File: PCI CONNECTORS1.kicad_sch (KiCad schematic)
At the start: 13 parts, among them J36 PCI1, J37 PCI1

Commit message: page 18 ISA, small fixes
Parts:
- removed J36, J37: PCI1, P2-3_ERA:PCI_GENERIC, symbol P2-3_era:PCI_Generic_1
- added J36, J37: PCI_CONN, custom:PCI1, symbol P2-3_era:PCI_Slot
- C18, C19, C20, C21: value 0.1uf 16v -> 0.1uf
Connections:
- net AD29 is gone; now on net AD1: R68.2
- net AD31 is gone; now on net AD1: R71.2
- net AD0: now also J36.A20 (AD(30)), J36.A22 (AD(28)), J36.A23 (AD(26)), J36.A25 (AD(24)), J36.A28 (AD(22)), J36.A29 (AD(20)), J36.A31 (AD(18)), J36.A32 (AD(16)), J36.A44 (AD(15)), J36.A46 (AD(13)), J36.A47 (AD(11)), J36.A49 (AD(09)), J36.A54 (AD(06)), J36.A55 (AD(04)), J36.A57 (AD(02)), J36.A58 (AD(00)), J37.A20 (AD(30)), J37.A22 (AD(28)), J37.A23 (AD(26)), J37.A25 (AD(24)), J37.A28 (AD(22)), J37.A29 (AD(20)), J37.A31 (AD(18)), J37.A32 (AD(16)), J37.A44 (AD(15)), J37.A46 (AD(13)), J37.A47 (AD(11)), J37.A49 (AD(09)), J37.A54 (AD(06)), J37.A55 (AD(04)), J37.A57 (AD(02)), J37.A58 (AD(00))
- net AD1: now also J36.B20 (AD(31)), J36.B21 (AD(29)), J36.B23 (AD(27)), J36.B24 (AD(25)), J36.B27 (AD(23)), J36.B29 (AD(21)), J36.B30 (AD(19)), J36.B32 (AD(17)), J36.B45 (AD(14)), J36.B47 (AD(12)), J36.B48 (AD(10)), J36.B52 (AD(8)), J36.B53 (AD(7)), J36.B55 (AD(5)), J36.B56 (AD(3)), J36.B58 (AD(1)), J37.B20 (AD(31)), J37.B21 (AD(29)), J37.B23 (AD(27)), J37.B24 (AD(25)), J37.B27 (AD(23)), J37.B29 (AD(21)), J37.B30 (AD(19)), J37.B32 (AD(17)), J37.B45 (AD(14)), J37.B47 (AD(12)), J37.B48 (AD(10)), J37.B52 (AD(8)), J37.B53 (AD(7)), J37.B55 (AD(5)), J37.B56 (AD(3)), J37.B58 (AD(1))
- net C/BE#(0): now also J36.A52 (C/BE#(0)), J37.A52 (C/BE#(0))
- net C/BE#(1): now also J36.B26 (C/BE#(3)), J36.B33 (C/BE#(2)), J36.B44 (C/BE#(1)), J37.B26 (C/BE#(3)), J37.B33 (C/BE#(2)), J37.B44 (C/BE#(1))
- net DEVSEL#: now also J36.B37 (DEVSEL#), J37.B37 (DEVSEL#)
- net FRAME#: now also J36.A34 (FRAME#), J37.A34 (FRAME#)
- net IRDY#: now also J36.B35 (IRDY#), J37.B35 (IRDY#)
- net PAR: now also J36.A43 (PAR), J37.A43 (PAR)
- net PCIRST#: now also J36.A15 (RESET#), J37.A15 (RESET#)
- net PCI_PME#: now also J36.A19 (PME#), J37.A19 (PME#)
- net PCLK3: now also J36.B16 (CLK)
- net PCLK4: now also J37.B16 (CLK)
- net PERR#: now also J36.B40 (PERR#), J37.B40 (PERR#)
- net PGNT#2: now also J36.A17 (GNT#)
- net PGNT#3: now also J37.A17 (GNT#)
- net PIRQ#A: now also J36.A7 (INTC#), J37.B7 (INTB#)
- net PIRQ#B: now also J36.B8 (INTD#), J37.A7 (INTC#)
- net PIRQ#C: now also J36.A6 (INTA#), J37.B8 (INTD#)
- net PIRQ#D: now also J36.B7 (INTB#), J37.A6 (INTA#)
- net PLOCK#: now also J36.B39 (LOCK#), J37.B39 (LOCK#)
- net PREQ#2: now also J36.B18 (REQ#)
- net PREQ#3: now also J37.B18 (REQ#)
- net PRSNT#31: now also J36.B9 (PRSNT1#)
- net PRSNT#32: now also J36.B11 (PRSNT2#)
- net PRSNT#41: now also J37.B9 (PRSNT1#)
- net PRSNT#42: now also J37.B11 (PRSNT2#)
- net PTCK: now also J36.B2 (TCK), J37.B2 (TCK)
- net PTDI: now also J36.A4 (TDI), J37.A4 (TDI)
- net PTMS: now also J36.A3 (TMS), J37.A3 (TMS)
- net PTRST#: now also J36.A1 (TRST#), J37.A1 (TRST#)
- net PU3_ACK64#: now also J36.A60 (REQ64#)
- net PU3_REQ64#: now also J36.B60 (ACK64#)
- net PU4_REQ64#: now also J37.B60 (ACK64#)
- net R_AD29: now also J36.A26 (IDSEL)
- net R_AD31: now also J37.A26 (IDSEL)
- net SBOP3: now also J36.A41 (SBO#)
- net SBOP4: now also J37.A41 (SBO#)
- net SDONEP3: now also J36.A40 (SDONE)
- net SDONEP4: now also J37.A40 (SDONE)
- net SERR#: now also J36.B42 (SERR#), J37.B42 (SERR#)
- net STOP#: now also J36.A38 (STOP#), J37.A38 (STOP#)
- net TRDY#: now also J36.A36 (TRDY#), J37.A36 (TRDY#)
- net Earth renamed GND
- net GND: now also J36.A12 (GND), J36.A13 (GND), J36.A18 (GND), J36.A24 (GND), J36.A30 (GND), J36.A35 (GND), J36.A37 (GND), J36.A42 (GND), J36.A48 (GND), J36.A56 (GND), J36.B12 (GND), J36.B13 (GND), J36.B15 (GND), J36.B17 (GND), J36.B22 (GND), J36.B28 (GND), J36.B3 (GND), J36.B34 (GND), J36.B38 (GND), J36.B46 (GND), J36.B49 (GND), J36.B57 (GND), J37.A12 (GND), J37.A13 (GND), J37.A18 (GND), J37.A24 (GND), J37.A30 (GND), J37.A35 (GND), J37.A37 (GND), J37.A42 (GND), J37.A48 (GND), J37.A56 (GND), J37.B12 (GND), J37.B13 (GND), J37.B15 (GND), J37.B17 (GND), J37.B22 (GND), J37.B28 (GND), J37.B3 (GND), J37.B34 (GND), J37.B38 (GND), J37.B46 (GND), J37.B49 (GND), J37.B57 (GND); no longer R70.2
- new net: J36.A10 (+5V), J36.A16 (+5V), J36.A5 (+5V), J36.A59 (+5V), J36.A61 (+5V), J36.A62 (+5V), J36.A8 (+5V)
- new net: J36.A21 (+3.3V), J36.A27 (+3.3V), J36.A33 (+3.3V), J36.A39 (+3.3V), J36.A45 (+3.3V), J36.A53 (+3.3V)
- new net: J36.B19 (+5V), J36.B5 (+5V), J36.B59 (+5V), J36.B6 (+5V), J36.B61 (+5V), J36.B62 (+5V)
- new net: J36.B25 (+3.3V), J36.B31 (+3.3V), J36.B36 (+3.3V), J36.B41 (+3.3V), J36.B43 (+3.3V), J36.B54 (+3.3V)
- new net: J37.A10 (+5V), J37.A16 (+5V), J37.A5 (+5V), J37.A59 (+5V), J37.A61 (+5V), J37.A62 (+5V), J37.A8 (+5V)
- new net: J37.A21 (+3.3V), J37.A27 (+3.3V), J37.A33 (+3.3V), J37.A39 (+3.3V), J37.A45 (+3.3V), J37.A53 (+3.3V)
- new net: J37.B19 (+5V), J37.B5 (+5V), J37.B59 (+5V), J37.B6 (+5V), J37.B61 (+5V), J37.B62 (+5V)
- new net: J37.B25 (+3.3V), J37.B31 (+3.3V), J37.B36 (+3.3V), J37.B41 (+3.3V), J37.B43 (+3.3V), J37.B54 (+3.3V)
- new net PU4_ACK64#: J37.A60 (REQ64#), R70.2
- no-connect marks 2 -> 12
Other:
- note added: "PCI CONNECTORS 3 AND 4"
- note removed: "PCI SLOTS 3 & 4"
- title: (none) -> PCI CONNECTORS 3 & 4
- moved on the sheet: C18, C19, C20, C21, R67, R68, R69, R70, R71, R72, RP3

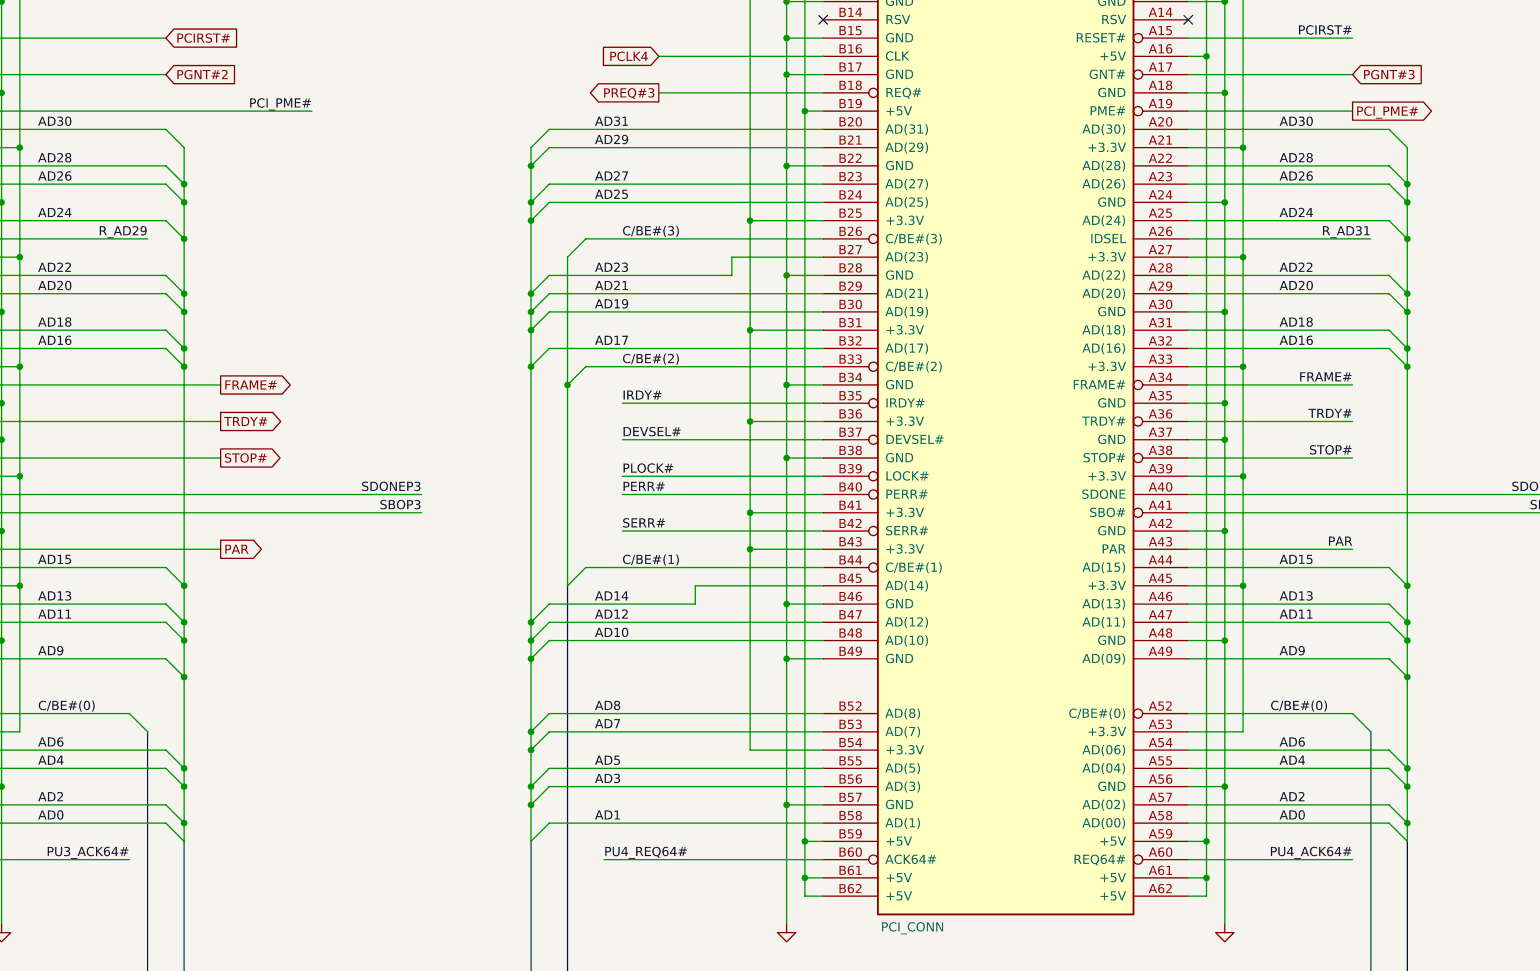
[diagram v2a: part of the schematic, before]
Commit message: page 6,7,8 82443BX chipset, various small fixes
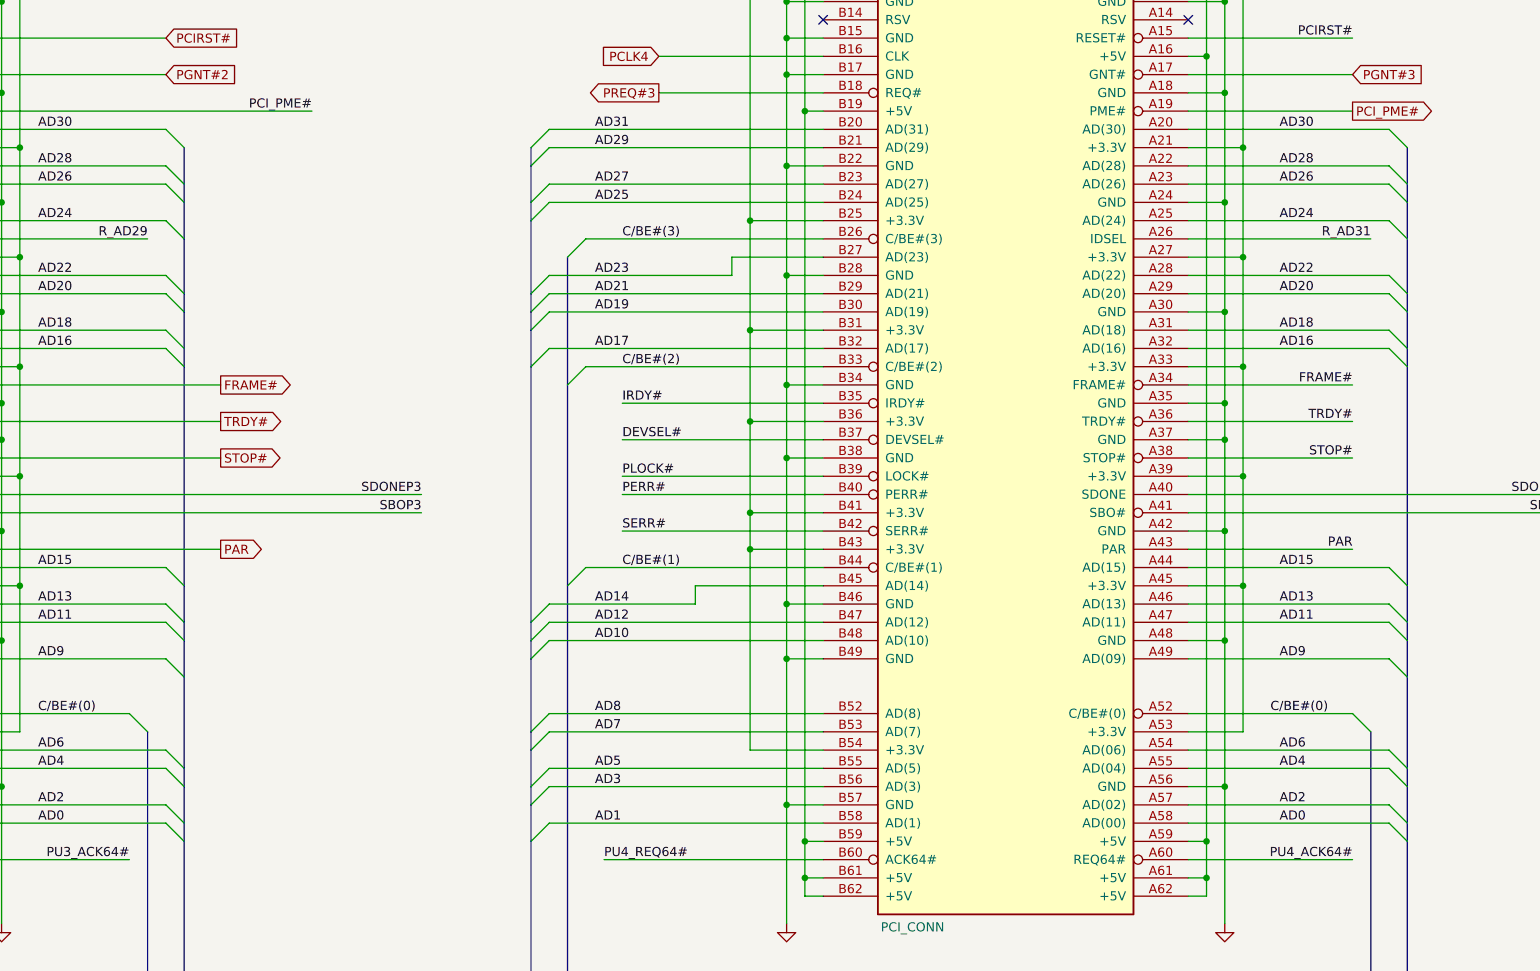
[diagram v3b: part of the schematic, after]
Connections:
- net AD0: no longer J36.A20 (AD(30)), J36.A22 (AD(28)), J36.A23 (AD(26)), J36.A25 (AD(24)), J36.A28 (AD(22)), J36.A29 (AD(20)), J36.A31 (AD(18)), J36.A32 (AD(16)), J36.A44 (AD(15)), J36.A46 (AD(13)), J36.A47 (AD(11)), J36.A49 (AD(09)), J36.A54 (AD(06)), J36.A55 (AD(04)), J36.A57 (AD(02)), J37.A20 (AD(30)), J37.A22 (AD(28)), J37.A23 (AD(26)), J37.A25 (AD(24)), J37.A28 (AD(22)), J37.A29 (AD(20)), J37.A31 (AD(18)), J37.A32 (AD(16)), J37.A44 (AD(15)), J37.A46 (AD(13)), J37.A47 (AD(11)), J37.A49 (AD(09)), J37.A54 (AD(06)), J37.A55 (AD(04)), J37.A57 (AD(02))
- net AD1: no longer J36.B20 (AD(31)), J36.B21 (AD(29)), J36.B23 (AD(27)), J36.B24 (AD(25)), J36.B27 (AD(23)), J36.B29 (AD(21)), J36.B30 (AD(19)), J36.B32 (AD(17)), J36.B45 (AD(14)), J36.B47 (AD(12)), J36.B48 (AD(10)), J36.B52 (AD(8)), J36.B53 (AD(7)), J36.B55 (AD(5)), J36.B56 (AD(3)), J37.B20 (AD(31)), J37.B21 (AD(29)), J37.B23 (AD(27)), J37.B24 (AD(25)), J37.B27 (AD(23)), J37.B29 (AD(21)), J37.B30 (AD(19)), J37.B32 (AD(17)), J37.B45 (AD(14)), J37.B47 (AD(12)), J37.B48 (AD(10)), J37.B52 (AD(8)), J37.B53 (AD(7)), J37.B55 (AD(5)), J37.B56 (AD(3)), R68.2, R71.2
- net C/BE#(1): no longer J36.B26 (C/BE#(3)), J36.B33 (C/BE#(2)), J37.B26 (C/BE#(3)), J37.B33 (C/BE#(2))
- new net AD10: J36.B48 (AD(10)), J37.B48 (AD(10))
- new net AD11: J36.A47 (AD(11)), J37.A47 (AD(11))
- new net AD12: J36.B47 (AD(12)), J37.B47 (AD(12))
- new net AD13: J36.A46 (AD(13)), J37.A46 (AD(13))
- new net AD14: J36.B45 (AD(14)), J37.B45 (AD(14))
- new net AD15: J36.A44 (AD(15)), J37.A44 (AD(15))
- new net AD16: J36.A32 (AD(16)), J37.A32 (AD(16))
- new net AD17: J36.B32 (AD(17)), J37.B32 (AD(17))
- new net AD18: J36.A31 (AD(18)), J37.A31 (AD(18))
- new net AD19: J36.B30 (AD(19)), J37.B30 (AD(19))
- new net AD2: J36.A57 (AD(02)), J37.A57 (AD(02))
- new net AD20: J36.A29 (AD(20)), J37.A29 (AD(20))
- new net AD21: J36.B29 (AD(21)), J37.B29 (AD(21))
- new net AD22: J36.A28 (AD(22)), J37.A28 (AD(22))
- new net AD23: J36.B27 (AD(23)), J37.B27 (AD(23))
- new net AD24: J36.A25 (AD(24)), J37.A25 (AD(24))
- new net AD25: J36.B24 (AD(25)), J37.B24 (AD(25))
- new net AD26: J36.A23 (AD(26)), J37.A23 (AD(26))
- new net AD27: J36.B23 (AD(27)), J37.B23 (AD(27))
- new net AD28: J36.A22 (AD(28)), J37.A22 (AD(28))
- new net AD29: J36.B21 (AD(29)), J37.B21 (AD(29)), R68.2
- new net AD3: J36.B56 (AD(3)), J37.B56 (AD(3))
- new net AD30: J36.A20 (AD(30)), J37.A20 (AD(30))
- new net AD31: J36.B20 (AD(31)), J37.B20 (AD(31)), R71.2
- new net AD4: J36.A55 (AD(04)), J37.A55 (AD(04))
- new net AD5: J36.B55 (AD(5)), J37.B55 (AD(5))
- new net AD6: J36.A54 (AD(06)), J37.A54 (AD(06))
- new net AD7: J36.B53 (AD(7)), J37.B53 (AD(7))
- new net AD8: J36.B52 (AD(8)), J37.B52 (AD(8))
- new net AD9: J36.A49 (AD(09)), J37.A49 (AD(09))
- new net C/BE#(2): J36.B33 (C/BE#(2)), J37.B33 (C/BE#(2))
- new net C/BE#(3): J36.B26 (C/BE#(3)), J37.B26 (C/BE#(3))
